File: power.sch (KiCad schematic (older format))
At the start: 0 parts

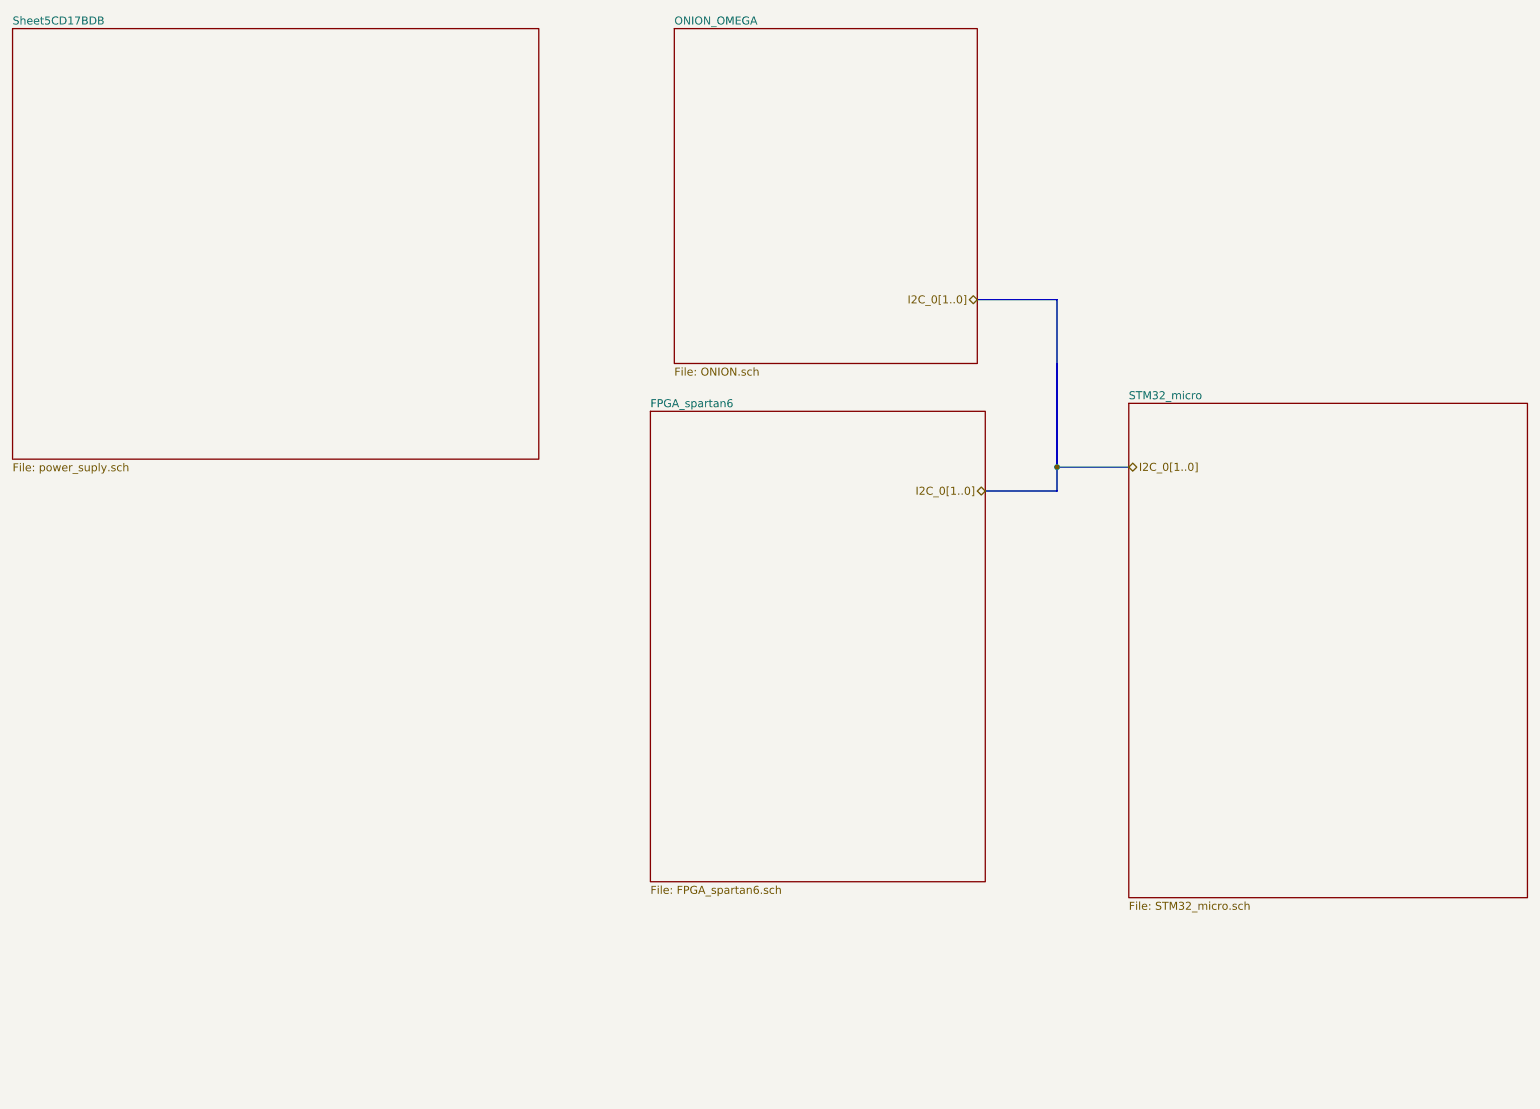
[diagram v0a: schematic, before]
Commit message: asignacion pines de control
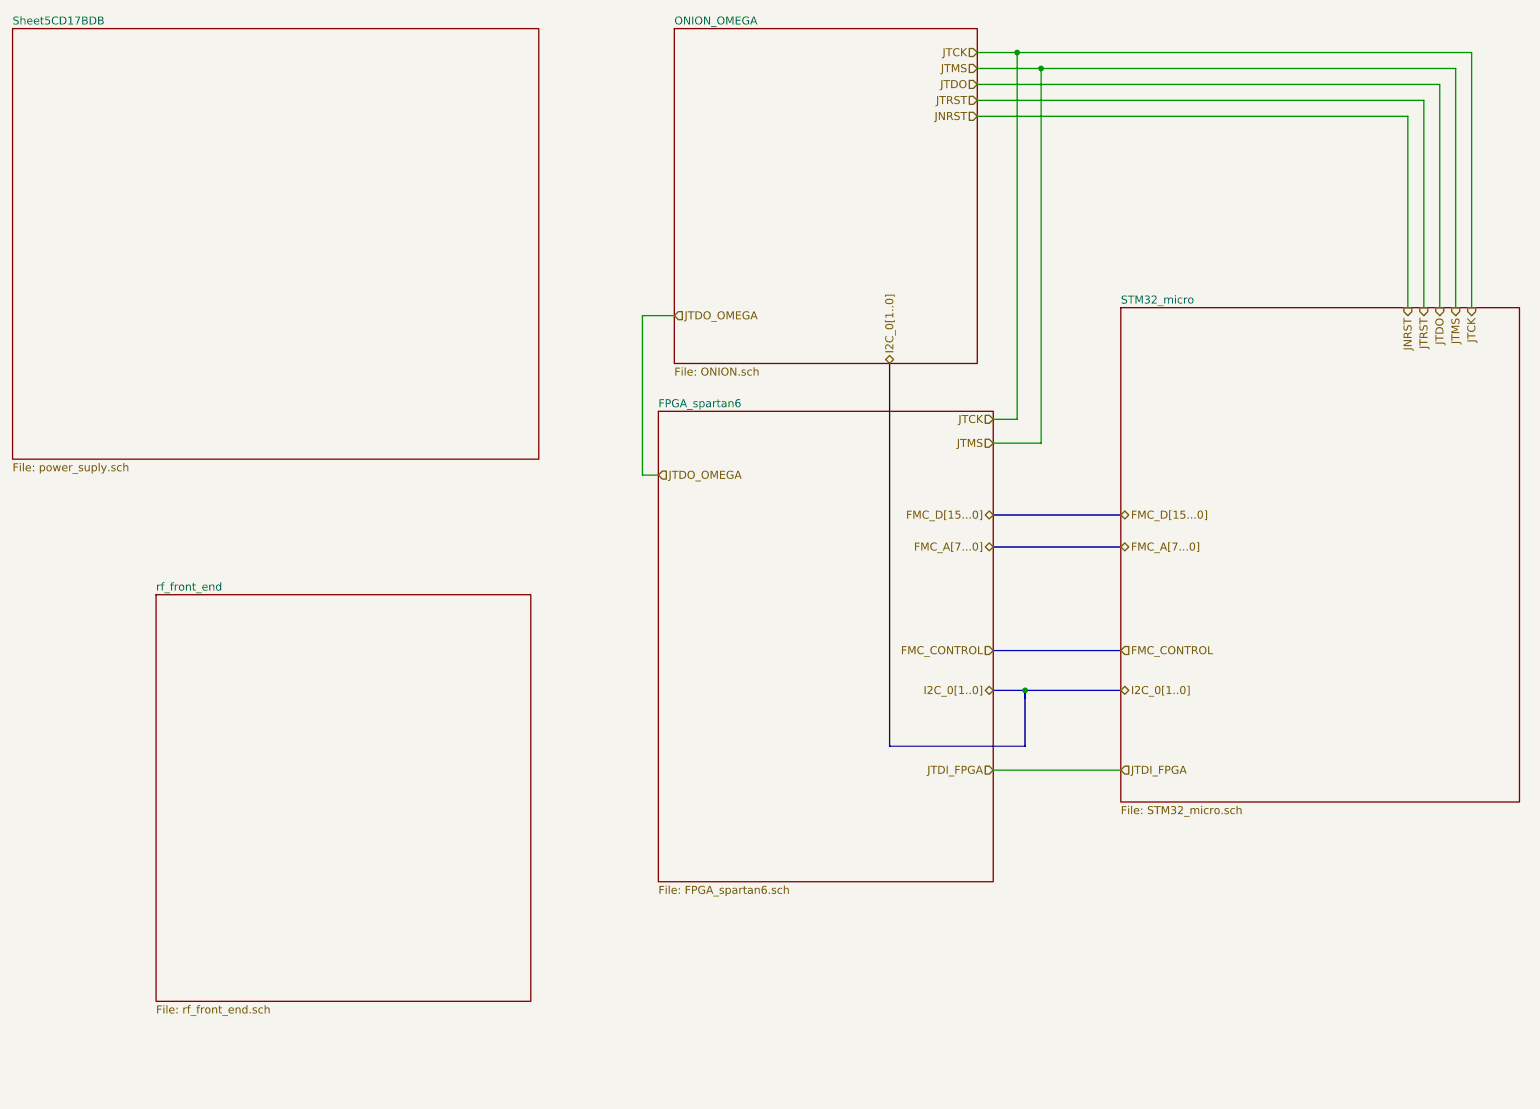
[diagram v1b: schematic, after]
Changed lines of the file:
@@
 $Descr A4 11693 8268
 encoding utf-8
-Sheet 1 5
+Sheet 1 6
 Title ""
 Date ""
@@
 $EndSheet
 $Sheet
-S 7750 3150 2500 3100
+S 7700 2550 2500 3100
 U 5CD05F2F
 F0 "STM32_micro" 50
@@
 F1 "ONION.sch" 50
 $EndSheet
-Text HLabel 6800 2500 0    50   BiDi ~ 0
+Text HLabel 6250 2900 1    50   BiDi ~ 0
 I2C_0[1..0]
-Text HLabel 7750 3550 2    50   BiDi ~ 0
+Text HLabel 7700 4950 2    50   BiDi ~ 0
 I2C_0[1..0]
-Text HLabel 6850 3700 0    50   BiDi ~ 0
+Text HLabel 6900 4950 0    50   BiDi ~ 0
 I2C_0[1..0]
-Wire Bus Line
-	6800 2500 7300 2500
-Wire Bus Line
-	7300 2500 7300 3550
-Wire Bus Line
-	7300 3700 6850 3700
-Wire Bus Line
-	7750 3550 7300 3550
-Connection ~ 7300 3550
-Wire Bus Line
-	7300 2900 7300 3550
 $Sheet
-S 4750 3200 2100 2950
+S 4800 3200 2100 2950
 U 5CF5B080
 F0 "FPGA_spartan6" 50
 F1 "FPGA_spartan6.sch" 50
 $EndSheet
+Text HLabel 6900 4700 0    50   Input ~ 0
+FMC_CONTROL
+Text HLabel 7700 4700 2    50   Input ~ 0
+FMC_CONTROL
+Text HLabel 6800 1150 0    50   Input ~ 0
+JTDO
+Text HLabel 6800 1050 0    50   Input ~ 0
+JTMS
+Text HLabel 6800 1250 0    50   Input ~ 0
+JTRST
+Text HLabel 6800 1350 0    50   Input ~ 0
+JNRST
+Text HLabel 9700 2550 3    50   Output ~ 0
+JTDO
+Text HLabel 9800 2550 3    50   Output ~ 0
+JTMS
+Text HLabel 9600 2550 3    50   Output ~ 0
+JTRST
+Text HLabel 9500 2550 3    50   Output ~ 0
+JNRST
+Text HLabel 6800 950  0    50   Input ~ 0
+JTCK
+Text HLabel 9900 2550 3    50   Output ~ 0
+JTCK
+Wire Wire Line
+	9900 950  9900 2550
+Wire Wire Line
+	9800 2550 9800 1050
+Wire Wire Line
+	9800 1050 7200 1050
+Wire Wire Line
+	6800 1150 9700 1150
+Wire Wire Line
+	9700 1150 9700 2550
+Wire Wire Line
+	9600 2550 9600 1250
+Wire Wire Line
+	9600 1250 6800 1250
+Wire Wire Line
+	6800 1350 9500 1350
+Wire Wire Line
+	9500 1350 9500 2550
+Text HLabel 7700 5450 2    50   Input ~ 0
+JTDI_FPGA
+Text HLabel 6900 5450 0    50   Input ~ 0
+JTDI_FPGA
+Text HLabel 4800 3600 2    50   Input ~ 0
+JTDO_OMEGA
+Text HLabel 4900 2600 2    50   Input ~ 0
+JTDO_OMEGA
 Wire Bus Line
-	7300 3550 7300 3700
+	7700 4700 6900 4700
+Wire Bus Line
+	6250 2900 6250 5300
+Wire Bus Line
+	6250 5300 7100 5300
+Wire Bus Line
+	7100 5300 7100 4950
+Wire Bus Line
+	7100 4950 6900 4950
+Wire Bus Line
+	7700 4950 7100 4950
+Wire Bus Line
+	7100 4950 7100 5000
+Connection ~ 7100 4950
+Wire Wire Line
+	7700 5450 6900 5450
+Wire Wire Line
+	4800 3600 4700 3600
+Wire Wire Line
+	4700 3600 4700 2600
+Wire Wire Line
+	4700 2600 4900 2600
+Text HLabel 6900 3400 0    50   Input ~ 0
+JTMS
+Text HLabel 6900 3250 0    50   Input ~ 0
+JTCK
+Wire Wire Line
+	7050 950  7050 3250
+Wire Wire Line
+	7050 3250 6900 3250
+Wire Wire Line
+	6800 950  7050 950
+Connection ~ 7050 950
+Wire Wire Line
+	7050 950  9900 950
+Wire Wire Line
+	7200 1050 7200 3400
+Wire Wire Line
+	7200 3400 6900 3400
+Connection ~ 7200 1050
+Wire Wire Line
+	7200 1050 6800 1050
+$Sheet
+S 1650 4350 2350 2550
+U 5DAC05CA
+F0 "rf_front_end" 50
+F1 "rf_front_end.sch" 50
+$EndSheet
+Text HLabel 6900 3850 0    50   BiDi ~ 0
+FMC_D[15...0]
+Text HLabel 7700 3850 2    50   BiDi ~ 0
+FMC_D[15...0]
+Wire Bus Line
+	6900 3850 7700 3850
+Text HLabel 6900 4050 0    50   BiDi ~ 0
+FMC_A[7...0]
+Text HLabel 7700 4050 2    50   BiDi ~ 0
+FMC_A[7...0]
+Wire Bus Line
+	6900 4050 7700 4050
 $EndSCHEMATC

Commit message: retoque casi finales
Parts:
- added H? (x4): MountingHole, MountingHole:MountingHole_2.7mm_M2.5_ISO14580_Pad, symbol Mechanical:MountingHole
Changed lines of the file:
@@
 Wire Bus Line
 	6900 4050 7700 4050
+$Comp
+L Mechanical:MountingHole H?
+U 0 0 5D41C458
+P 2000 7400
+F 0 "H?" H 2100 7446 50  0000 L CNN
+F 1 "MountingHole" H 2100 7355 50  0000 L CNN
+F 2 "MountingHole:MountingHole_2.7mm_M2.5_ISO14580_Pad" H 2000 7400 50  0001 C CNN
+F 3 "~" H 2000 7400 50  0001 C CNN
+	0    2000 7400
+	1    0    0    -1
+$EndComp
+$Comp
+L Mechanical:MountingHole H?
+U 0 0 5D41F16D
+P 2800 7400
+F 0 "H?" H 2900 7446 50  0000 L CNN
+F 1 "MountingHole" H 2900 7355 50  0000 L CNN
+F 2 "MountingHole:MountingHole_2.7mm_M2.5_ISO14580_Pad" H 2800 7400 50  0001 C CNN
+F 3 "~" H 2800 7400 50  0001 C CNN
+	0    2800 7400
+	1    0    0    -1
+$EndComp
+$Comp
+L Mechanical:MountingHole H?
+U 0 0 5D41F6A8
+P 3600 7400
+F 0 "H?" H 3700 7446 50  0000 L CNN
+F 1 "MountingHole" H 3700 7355 50  0000 L CNN
+F 2 "MountingHole:MountingHole_2.7mm_M2.5_ISO14580_Pad" H 3600 7400 50  0001 C CNN
+F 3 "~" H 3600 7400 50  0001 C CNN
+	0    3600 7400
+	1    0    0    -1
+$EndComp
+$Comp
+L Mechanical:MountingHole H?
+U 0 0 5D41FACE
+P 4400 7400
+F 0 "H?" H 4500 7446 50  0000 L CNN
+F 1 "MountingHole" H 4500 7355 50  0000 L CNN
+F 2 "MountingHole:MountingHole_2.7mm_M2.5_ISO14580_Pad" H 4400 7400 50  0001 C CNN
+F 3 "~" H 4400 7400 50  0001 C CNN
+	0    4400 7400
+	1    0    0    -1
+$EndComp
 $EndSCHEMATC

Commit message: diseño de esquematico
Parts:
- gave numbers to parts that had none: 4
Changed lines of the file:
@@
 	6900 4050 7700 4050
 $Comp
-L Mechanical:MountingHole H?
-U 0 0 5D41C458
+L Mechanical:MountingHole H1
+U 1 1 5D41C458
 P 2000 7400
-F 0 "H?" H 2100 7446 50  0000 L CNN
+F 0 "H1" H 2100 7446 50  0000 L CNN
 F 1 "MountingHole" H 2100 7355 50  0000 L CNN
 F 2 "MountingHole:MountingHole_2.7mm_M2.5_ISO14580_Pad" H 2000 7400 50  0001 C CNN
 F 3 "~" H 2000 7400 50  0001 C CNN
-	0    2000 7400
+	1    2000 7400
 	1    0    0    -1
 $EndComp
 $Comp
-L Mechanical:MountingHole H?
-U 0 0 5D41F16D
+L Mechanical:MountingHole H2
+U 1 1 5D41F16D
 P 2800 7400
-F 0 "H?" H 2900 7446 50  0000 L CNN
+F 0 "H2" H 2900 7446 50  0000 L CNN
 F 1 "MountingHole" H 2900 7355 50  0000 L CNN
 F 2 "MountingHole:MountingHole_2.7mm_M2.5_ISO14580_Pad" H 2800 7400 50  0001 C CNN
 F 3 "~" H 2800 7400 50  0001 C CNN
-	0    2800 7400
+	1    2800 7400
 	1    0    0    -1
 $EndComp
 $Comp
-L Mechanical:MountingHole H?
-U 0 0 5D41F6A8
+L Mechanical:MountingHole H3
+U 1 1 5D41F6A8
 P 3600 7400
-F 0 "H?" H 3700 7446 50  0000 L CNN
+F 0 "H3" H 3700 7446 50  0000 L CNN
 F 1 "MountingHole" H 3700 7355 50  0000 L CNN
 F 2 "MountingHole:MountingHole_2.7mm_M2.5_ISO14580_Pad" H 3600 7400 50  0001 C CNN
 F 3 "~" H 3600 7400 50  0001 C CNN
-	0    3600 7400
+	1    3600 7400
 	1    0    0    -1
 $EndComp
 $Comp
-L Mechanical:MountingHole H?
-U 0 0 5D41FACE
+L Mechanical:MountingHole H4
+U 1 1 5D41FACE
 P 4400 7400
-F 0 "H?" H 4500 7446 50  0000 L CNN
+F 0 "H4" H 4500 7446 50  0000 L CNN
 F 1 "MountingHole" H 4500 7355 50  0000 L CNN
 F 2 "MountingHole:MountingHole_2.7mm_M2.5_ISO14580_Pad" H 4400 7400 50  0001 C CNN
 F 3 "~" H 4400 7400 50  0001 C CNN
-	0    4400 7400
+	1    4400 7400
 	1    0    0    -1
 $EndComp
